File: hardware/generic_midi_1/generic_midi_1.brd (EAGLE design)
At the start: 47.9 x 45.4 mm, 20 parts, among them IC1 MEGA48/88/168-PU, IC2 RFM12

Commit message: Changed microcontroller name to MEGA168/328
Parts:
- IC1: value MEGA48/88/168-PU -> MEGA168/328
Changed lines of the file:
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@@
 <?xml version="1.0" encoding="utf-8"?>
 <!DOCTYPE eagle SYSTEM "eagle.dtd">
-<eagle version="6.2">
+<eagle version="6.4">
 <drawing>
 <settings>
@@
 <layer number="23" name="tOrigins" color="15" fill="1" visible="yes" active="yes"/>
 <layer number="24" name="bOrigins" color="15" fill="1" visible="yes" active="yes"/>
-<layer number="25" name="tNames" color="7" fill="1" visible="no" active="yes"/>
-<layer number="26" name="bNames" color="7" fill="1" visible="no" active="yes"/>
-<layer number="27" name="tValues" color="7" fill="1" visible="no" active="yes"/>
-<layer number="28" name="bValues" color="7" fill="1" visible="no" active="yes"/>
-<layer number="29" name="tStop" color="7" fill="3" visible="no" active="yes"/>
-<layer number="30" name="bStop" color="7" fill="6" visible="no" active="yes"/>
-<layer number="31" name="tCream" color="7" fill="4" visible="no" active="yes"/>
-<layer number="32" name="bCream" color="7" fill="5" visible="no" active="yes"/>
-<layer number="33" name="tFinish" color="6" fill="3" visible="no" active="yes"/>
-<layer number="34" name="bFinish" color="6" fill="6" visible="no" active="yes"/>
-<layer number="35" name="tGlue" color="7" fill="4" visible="no" active="yes"/>
-<layer number="36" name="bGlue" color="7" fill="5" visible="no" active="yes"/>
-<layer number="37" name="tTest" color="7" fill="1" visible="no" active="yes"/>
-<layer number="38" name="bTest" color="7" fill="1" visible="no" active="yes"/>
-<layer number="39" name="tKeepout" color="4" fill="11" visible="no" active="yes"/>
-<layer number="40" name="bKeepout" color="1" fill="11" visible="no" active="yes"/>
-<layer number="41" name="tRestrict" color="4" fill="10" visible="no" active="yes"/>
-<layer number="42" name="bRestrict" color="1" fill="10" visible="no" active="yes"/>
-<layer number="43" name="vRestrict" color="2" fill="10" visible="no" active="yes"/>
-<layer number="44" name="Drills" color="7" fill="1" visible="no" active="yes"/>
-<layer number="45" name="Holes" color="7" fill="1" visible="no" active="yes"/>
-<layer number="46" name="Milling" color="3" fill="1" visible="no" active="yes"/>
-<layer number="47" name="Measures" color="7" fill="1" visible="no" active="yes"/>
-<layer number="48" name="Document" color="7" fill="1" visible="no" active="yes"/>
-<layer number="49" name="Reference" color="7" fill="1" visible="no" active="yes"/>
+<layer number="25" name="tNames" color="7" fill="1" visible="yes" active="yes"/>
+<layer number="26" name="bNames" color="7" fill="1" visible="yes" active="yes"/>
+<layer number="27" name="tValues" color="7" fill="1" visible="yes" active="yes"/>
+<layer number="28" name="bValues" color="7" fill="1" visible="yes" active="yes"/>
+<layer number="29" name="tStop" color="7" fill="3" visible="yes" active="yes"/>
+<layer number="30" name="bStop" color="7" fill="6" visible="yes" active="yes"/>
+<layer number="31" name="tCream" color="7" fill="4" visible="yes" active="yes"/>
+<layer number="32" name="bCream" color="7" fill="5" visible="yes" active="yes"/>
+<layer number="33" name="tFinish" color="6" fill="3" visible="yes" active="yes"/>
+<layer number="34" name="bFinish" color="6" fill="6" visible="yes" active="yes"/>
+<layer number="35" name="tGlue" color="7" fill="4" visible="yes" active="yes"/>
+<layer number="36" name="bGlue" color="7" fill="5" visible="yes" active="yes"/>
+<layer number="37" name="tTest" color="7" fill="1" visible="yes" active="yes"/>
+<layer number="38" name="bTest" color="7" fill="1" visible="yes" active="yes"/>
+<layer number="39" name="tKeepout" color="4" fill="11" visible="yes" active="yes"/>
+<layer number="40" name="bKeepout" color="1" fill="11" visible="yes" active="yes"/>
+<layer number="41" name="tRestrict" color="4" fill="10" visible="yes" active="yes"/>
+<layer number="42" name="bRestrict" color="1" fill="10" visible="yes" active="yes"/>
+<layer number="43" name="vRestrict" color="2" fill="10" visible="yes" active="yes"/>
+<layer number="44" name="Drills" color="7" fill="1" visible="yes" active="yes"/>
+<layer number="45" name="Holes" color="7" fill="1" visible="yes" active="yes"/>
+<layer number="46" name="Milling" color="3" fill="1" visible="yes" active="yes"/>
+<layer number="47" name="Measures" color="7" fill="1" visible="yes" active="yes"/>
+<layer number="48" name="Document" color="7" fill="1" visible="yes" active="yes"/>
+<layer number="49" name="Reference" color="7" fill="1" visible="yes" active="yes"/>
 <layer number="50" name="dxf" color="7" fill="1" visible="no" active="no"/>
-<layer number="51" name="tDocu" color="7" fill="1" visible="no" active="yes"/>
-<layer number="52" name="bDocu" color="7" fill="1" visible="no" active="yes"/>
+<layer number="51" name="tDocu" color="7" fill="1" visible="yes" active="yes"/>
+<layer number="52" name="bDocu" color="7" fill="1" visible="yes" active="yes"/>
 <layer number="91" name="Nets" color="2" fill="1" visible="no" active="no"/>
 <layer number="92" name="Busses" color="1" fill="1" visible="no" active="no"/>
@@
 </class>
 </classes>
-<designrules>
+<designrules name="default">
 <description language="de">&lt;b&gt;EAGLE Design Rules&lt;/b&gt;
 &lt;p&gt;
@@
 <element name="IC2" library="hopeRF" package="RFM" value="RFM12" x="64.77" y="66.04" rot="MR180"/>
 <element name="LED1" library="led" package="LED3MM" value="2mA" x="67.945" y="29.21" rot="R270"/>
-<element name="IC1" library="avr-5-4.16" package="DIL28-3" value="MEGA48/88/168-PU" x="63.5" y="38.1"/>
+<element name="IC1" library="avr-5-4.16" package="DIL28-3" value="MEGA168/328" x="63.5" y="38.1"/>
 <element name="JP1" library="avr-5-4.16" package="AVR-ISP-6" value="AVR-ISP-6" x="52.705" y="64.135" rot="R180"/>
 <element name="R1" library="rcl" package="0207/7" value="560R" x="73.66" y="31.75" rot="R180"/>

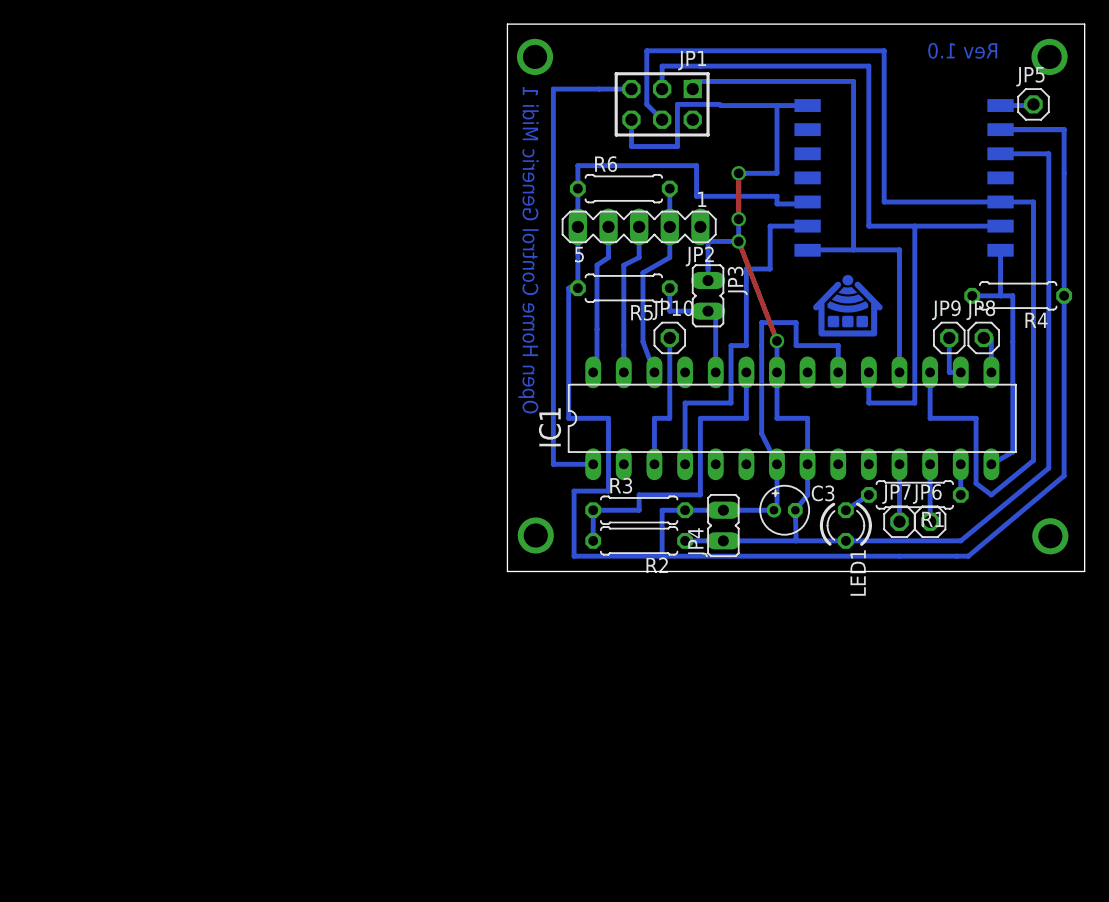
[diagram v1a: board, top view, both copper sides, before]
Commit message: renames connectors, changed positions of labels, updated mask, placing and partlist
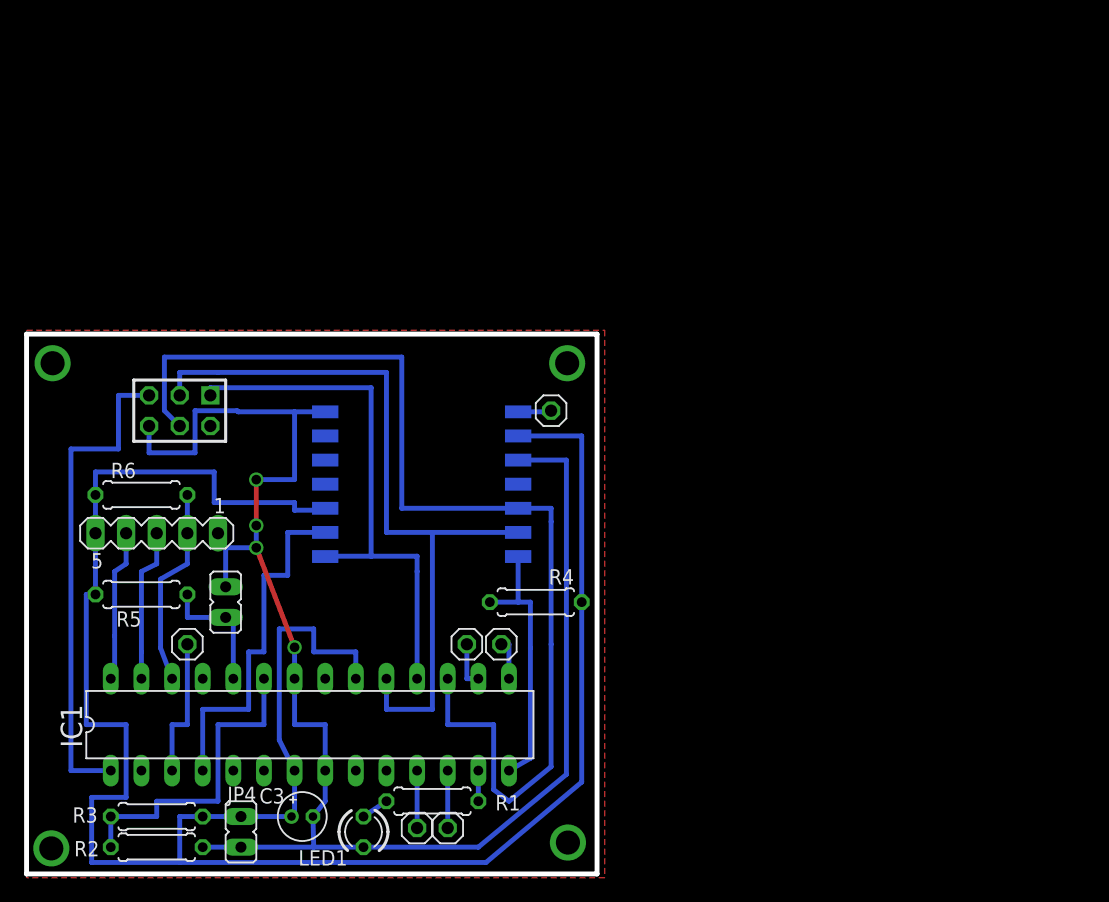
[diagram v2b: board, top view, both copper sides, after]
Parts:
- JP10: value PD5 -> PD6
- JP6: value PD6 -> PB1
- JP7: value PD5 -> PB2
- JP8: value PB1 -> PD5
- JP9: value PB2 -> PD5
- moved JP8 70.8 mm to (13.3, 19.4)
- moved JP9 60.0 mm to (32.4, 4.13)
- moved C3 47.4 mm to (22.9, 5.08)
- moved R4 47.4 mm to (42.2, 22.9)
- moved R5 47.4 mm to (9.53, 23.5)
- moved R6 47.4 mm to (9.53, 31.8)
- moved IC1 47.4 mm to (23.5, 12.7)
- moved IC2 47.4 mm to (24.8, 40.6)
- moved JP1 47.4 mm to (12.7, 38.7)
- moved JP2 47.4 mm to (10.8, 28.6)
- moved JP3 47.4 mm to (16.5, 22.9)
- moved JP4 47.4 mm to (17.8, 3.81)
- moved JP5 47.4 mm to (43.5, 38.7)
- moved LED1 47.4 mm to (27.9, 3.81)
- moved R1 47.4 mm to (33.7, 6.35)
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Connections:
- net N$14: now also JP9.1; no longer JP7.1
- net N$16: now also JP10.1; no longer JP6.1
- net N$17: now also JP6.1; no longer JP8.1
- net N$19: now also JP7.1; no longer JP9.1
- net N$20: now also JP8.1; no longer JP10.1
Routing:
- net VCC: track 184.5 -> 179.1 mm
- added copper zone on layer 1, net GND
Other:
- board size 47.9 x 45.4 mm -> 47.3 x 44.8 mm
- board text added: "D:/Eigene Dateien/ohc/logo/logo_black 150x133.bmp"
